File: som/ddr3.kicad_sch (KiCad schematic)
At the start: 10 parts, among them U2 AS4C256M16D3, U3 AS4C256M16D3

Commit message: Le DDR3 control traces
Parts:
- C1, C2: footprint Capacitor_SMD:C_0402_1005Metric_Pad0.74x0.62mm_HandSolder -> Capacitor_SMD:C_0402_1005Metric
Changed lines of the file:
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@@
 			)
 		)
-		(property "Footprint" "Capacitor_SMD:C_0402_1005Metric_Pad0.74x0.62mm_HandSolder"
+		(property "Footprint" "Capacitor_SMD:C_0402_1005Metric"
 			(at 147.32 49.53 0)
 			(effects
@@
 			)
 		)
-		(property "Footprint" "Capacitor_SMD:C_0402_1005Metric_Pad0.74x0.62mm_HandSolder"
+		(property "Footprint" "Capacitor_SMD:C_0402_1005Metric"
 			(at 81.28 49.53 0)
 			(effects

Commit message: DDR3 (again)
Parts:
- removed R6, R7, R8, R9: 10k, Resistor_SMD:R_0402_1005Metric_Pad0.72x0.64mm_HandSolder, symbol Device:R_Small
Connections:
- net DDR_VREF: now reaches C2.1, U2.H1 (VREFDQ), U2.M8 (VREFCA)
- net DDR_VREF: now also C1.1, U3.H1 (VREFDQ), U3.M8 (VREFCA)
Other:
- moved on the sheet: C1, C2

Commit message: I really should commit when I make it and not a month later
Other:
- note added: "DDR3L Configuration: 256K*32 Speed: 800 MT/s Impedance: 40 ohm"
- moved on the sheet: C1, C2, R1, R2, U2, U3

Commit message: ok
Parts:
- added C100: 4.7uF, Capacitor_SMD:C_0402_1005Metric, symbol Device:C_Small
- added C97, C99: 100nF, Capacitor_SMD:C_0402_1005Metric, symbol Device:C_Small
- added C98: 1nF, Capacitor_SMD:C_0402_1005Metric, symbol Device:C_Small
- added R17, R18: 10K, Resistor_SMD:R_0402_1005Metric_Pad0.72x0.64mm_HandSolder, symbol Device:R_Small
- added RN1, RN2, RN3, RN4, RN5, RN6, RN7: R_Pack04, Resistor_SMD:R_Array_Concave_4x0402, symbol Device:R_Pack04
- added U9: TPS51200DRC, Package_SON:VSON-10-1EP_3x3mm_P0.5mm_EP1.65x2.4mm, symbol Regulator_Linear:TPS51200DRC
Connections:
- net +1V35: now also R17.2, U9.2 (VLDOIN)
- net DDR_A0: now also RN5.7 (R2.2)
- net DDR_A1: now also RN1.8 (R1.2)
- net DDR_A10: now also RN3.5 (R4.2)
- net DDR_A11: now also RN1.6 (R3.2)
- net DDR_A12: now also RN2.8 (R1.2)
- net DDR_A13: now also RN4.8 (R1.2)
- net DDR_A14: now also RN1.5 (R4.2)
- net DDR_A2: now also RN4.5 (R4.2)
- net DDR_A3: now also RN5.6 (R3.2)
- net DDR_A4: now also RN2.6 (R3.2)
- net DDR_A5: now also RN5.8 (R1.2)
- net DDR_A6: now also RN2.5 (R4.2)
- net DDR_A7: now also RN4.6 (R3.2)
- net DDR_A8: now also RN1.7 (R2.2)
- net DDR_A9: now also RN4.7 (R2.2)
- net DDR_BA0: now also RN5.5 (R4.2)
- net DDR_BA1: now also RN2.7 (R2.2)
- net DDR_BA2: now also RN6.8 (R1.2)
- net DDR_CLK+: now also RN3.8 (R1.2)
- net DDR_CLK-: now also RN3.7 (R2.2)
- net DDR_CLK_E: now also RN3.6 (R3.2)
- net DDR_ODT: now also RN6.6 (R3.2)
- net DDR_VREF: now also C99.2, U9.6 (REFOUT)
- net GND: now also C100.1, C98.2, C99.1, R18.2, U9.11 (GND), U9.4 (GND), U9.8 (GND)
- net ~{DDR_CAS}: now also RN7.7 (R2.2)
- net ~{DDR_CS}: now also RN6.7 (R2.2)
- net ~{DDR_RAS}: now also RN7.8 (R1.2)
- net ~{DDR_WE}: now also RN7.6 (R3.2)
- new net: C98.1, R17.1, R18.1, U9.1 (REFIN)
- new net: C97.1, RN3.1 (R1.1), RN3.2 (R2.1)
- new net +3V3: C100.2, U9.10 (VIN), U9.7 (EN)
- new net V_{TT}: C97.2, RN1.1 (R1.1), RN1.2 (R2.1), RN1.3 (R3.1), RN1.4 (R4.1), RN2.1 (R1.1), RN2.2 (R2.1), RN2.3 (R3.1), RN2.4 (R4.1), RN3.3 (R3.1), RN3.4 (R4.1), RN4.1 (R1.1), RN4.2 (R2.1), RN4.3 (R3.1), RN4.4 (R4.1), RN5.1 (R1.1), RN5.2 (R2.1), RN5.3 (R3.1), RN5.4 (R4.1), RN6.1 (R1.1), RN6.2 (R2.1), RN6.3 (R3.1), RN7.1 (R1.1), RN7.2 (R2.1), RN7.3 (R3.1), U9.3 (VO), U9.5 (VOSNS)
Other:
- note added: "DDR3L Configuration: 256K*32 Speed: 800 MT/s Impedance: 40 ohm Termination: 40 ohm AC termination: 40 ohm, 100nF"
- note removed: "DDR3L Configuration: 256K*32 Speed: 800 MT/s Impedance: 40 ohm"
- moved on the sheet: C1, C2, R1, R2, U2, U3

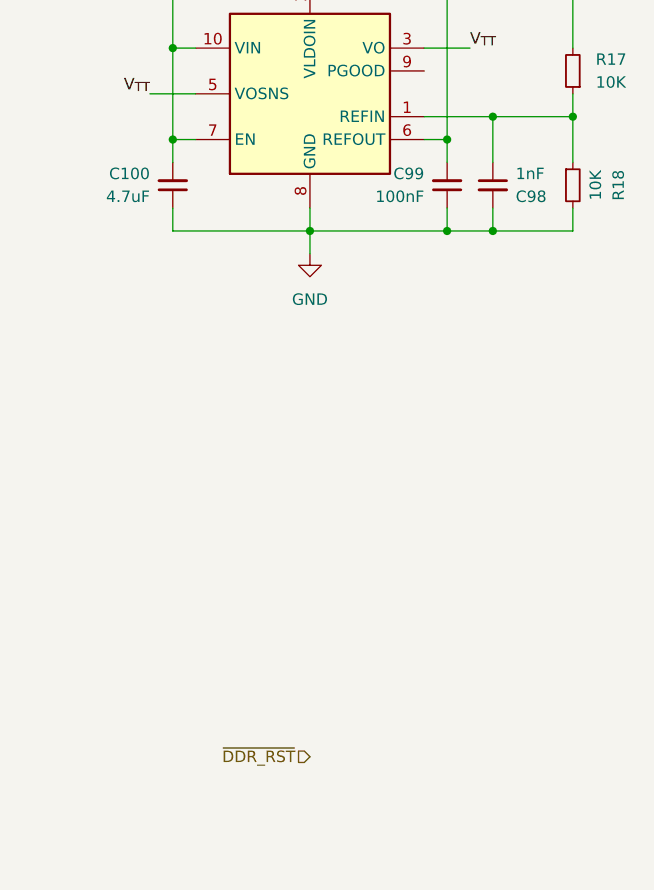
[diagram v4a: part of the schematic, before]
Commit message: Work on GTP and power supplies for it
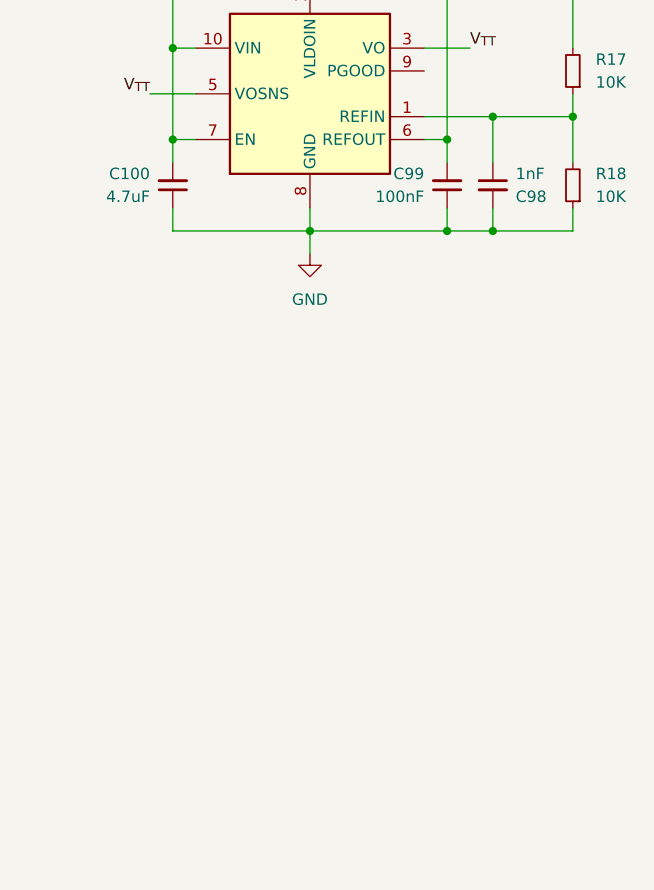
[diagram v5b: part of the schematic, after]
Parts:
- R17, R18: footprint Resistor_SMD:R_0402_1005Metric_Pad0.72x0.64mm_HandSolder -> Resistor_SMD:R_0402_1005Metric
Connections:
- net GND: now also R18.1; no longer R18.2
- net at C98.1, R17.1, U9.1 (REFIN): now also R18.2; no longer R18.1
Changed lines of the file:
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@@
-		)
-	)
-	(hierarchical_label "~{DDR_RST}"
-		(shape input)
-		(at 240.03 138.43 180)
-		(fields_autoplaced yes)
-		(effects
-			(font
-				(size 1.27 1.27)
-			)
-			(justify right)
 		)
 	)
@@
 	)
 	(symbol
+		(lib_id "Device:R_Small")
+		(at 269.24 74.93 180)
+		(unit 1)
+		(exclude_from_sim no)
+		(in_bom yes)
+		(on_board yes)
+		(dnp no)
+		(property "Reference" "R18"
+			(at 271.78 73.6599 0)
+			(effects
+				(font
+					(size 1.27 1.27)
+				)
+				(justify right)
+			)
+		)
+		(property "Value" "10K"
+			(at 271.78 76.1999 0)
+			(effects
+				(font
+					(size 1.27 1.27)
+				)
+				(justify right)
+			)
+		)
+		(property "Footprint" "Resistor_SMD:R_0402_1005Metric"
+			(at 269.24 74.93 0)
+			(effects
+				(font
+					(size 1.27 1.27)
+				)
+				(hide yes)
+			)
+		)
+		(property "Datasheet" "~"
+			(at 269.24 74.93 0)
+			(effects
+				(font
+					(size 1.27 1.27)
+				)
+				(hide yes)
+			)
+		)
+		(property "Description" "Resistor, small symbol"
+			(at 269.24 74.93 0)
+			(effects
+				(font
+					(size 1.27 1.27)
+				)
+				(hide yes)
+			)
+		)
+		(pin "2"
+		)
+		(pin "1"
+		)
+		(instances
+			(project "pixieboard"
+				(path "/e7142f2b-5d92-4ad9-8024-bfc94c5783c1/57afc700-82e6-45de-a8f3-81fb003e9961"
+					(reference "R18")
+					(unit 1)
+				)
+			)
+		)
+	)
+	(symbol
 		(lib_id "Device:R_Pack04")
 		(at 181.61 63.5 90)
@@
 			)
 		)
-		(property "Footprint" "Resistor_SMD:R_0402_1005Metric_Pad0.72x0.64mm_HandSolder"
+		(property "Footprint" "Resistor_SMD:R_0402_1005Metric"
 			(at 269.24 62.23 0)
 			(effects
@@
 					(unit 1)
 				)
-			)
-		)
-	)
-	(symbol
-		(lib_id "Device:R_Small")
-		(at 269.24 74.93 0)
-		(unit 1)
-		(exclude_from_sim no)
-		(in_bom yes)
-		(on_board yes)
-		(dnp no)
-		(property "Reference" "R18"
-			(at 274.32 74.93 90)
-			(effects
-				(font
-					(size 1.27 1.27)
-				)
-			)
-		)
-		(property "Value" "10K"
-			(at 271.78 74.93 90)
-			(effects
-				(font
-					(size 1.27 1.27)
-				)
-			)
-		)
-		(property "Footprint" "Resistor_SMD:R_0402_1005Metric_Pad0.72x0.64mm_HandSolder"
-			(at 269.24 74.93 0)
-			(effects
-				(font
-					(size 1.27 1.27)
-				)
-				(hide yes)
-			)
-		)
-		(property "Datasheet" "~"
-			(at 269.24 74.93 0)
-			(effects
-				(font
-					(size 1.27 1.27)
-				)
-				(hide yes)
-			)
-		)
-		(property "Description" "Resistor, small symbol"
-			(at 269.24 74.93 0)
-			(effects
-				(font
-					(size 1.27 1.27)
-				)
-				(hide yes)
-			)
-		)
-		(pin "2"
-		)
-		(pin "1"
-		)
-		(instances
-			(project "pixieboard"
-				(path "/e7142f2b-5d92-4ad9-8024-bfc94c5783c1/57afc700-82e6-45de-a8f3-81fb003e9961"
-					(reference "R18")
-					(unit 1)
-				)

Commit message: idk
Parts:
- RN1, RN2, RN3, RN4, RN5, RN6, RN7: LCSC part number (none) -> C136844
- U2, U3: LCSC part number (none) -> C2982171
- U9: LCSC part number (none) -> C34771
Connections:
- net V_{TT}: now also RN7.4 (R4.1)
- net ~{DDR_RST}: now also RN7.5 (R4.2)
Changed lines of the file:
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@@
 	)
 	(junction
+		(at 196.85 137.16)
+		(diameter 0)
+		(color 0 0 0 0)
+	)
+	(junction
 		(at 196.85 63.5)
 		(diameter 0)
@@
 	(wire
 		(pts
+			(xy 196.85 137.16) (xy 196.85 139.7)
+		)
+		(stroke
+			(width 0)
+			(type default)
+		)
+	)
+	(wire
+		(pts
 			(xy 196.85 101.6) (xy 196.85 104.14)
 		)
@@
 	(wire
 		(pts
-			(xy 196.85 132.08) (xy 196.85 139.7)
+			(xy 196.85 132.08) (xy 196.85 137.16)
 		)
 		(stroke
@@
 	(wire
 		(pts
+			(xy 186.69 137.16) (xy 196.85 137.16)
+		)
+		(stroke
+			(width 0)
+			(type default)
+		)
+	)
+	(wire
+		(pts
 			(xy 54.61 53.34) (xy 54.61 55.88)
 		)
@@
 		)
 	)
+	(hierarchical_label "~{DDR_RST}"
+		(shape input)
+		(at 176.53 137.16 180)
+		(fields_autoplaced yes)
+		(effects
+			(font
+				(size 1.27 1.27)
+			)
+			(justify right)
+		)
+	)
 	(hierarchical_label "DDR_A11"
 		(shape input)
@@
 			)
 		)
+		(property "LCSC part number" "C2982171"
+			(at 49.53 99.06 0)
+			(effects
+				(font
+					(size 1.27 1.27)
+				)
+				(hide yes)
+			)
+		)
 		(pin "C2"
 		)
@@
 			)
 		)
+		(property "LCSC part number" "C34771"
+			(at 240.03 64.77 0)
+			(effects
+				(font
+					(size 1.27 1.27)
+				)
+				(hide yes)
+			)
+		)
 		(pin "7"
 		)
@@
 			)
 		)
+		(property "LCSC part number" "C136844"
+			(at 181.61 63.5 90)
+			(effects
+				(font
+					(size 1.27 1.27)
+				)
+				(hide yes)
+			)
+		)
 		(pin "6"
 		)
@@
 			)
 		)
+		(property "LCSC part number" "C136844"
+			(at 181.61 114.3 90)
+			(effects
+				(font
+					(size 1.27 1.27)
+				)
+				(hide yes)
+			)
+		)
 		(pin "6"
 		)
@@
 			)
 		)
+		(property "LCSC part number" "C136844"
+			(at 181.61 76.2 90)
+			(effects
+				(font
+					(size 1.27 1.27)
+				)
+				(hide yes)
+			)
+		)
 		(pin "6"
 		)
@@
 			)
 		)
+		(property "LCSC part number" "C136844"
+			(at 181.61 127 90)
+			(effects
+				(font
+					(size 1.27 1.27)
+				)
+				(hide yes)
+			)
+		)
 		(pin "6"
 		)
@@
 			)
 		)
+		(property "LCSC part number" "C136844"
+			(at 181.61 88.9 90)
+			(effects
+				(font
+					(size 1.27 1.27)
+				)
+				(hide yes)
+			)
+		)
 		(pin "6"
 		)
@@
 			)
 		)
+		(property "LCSC part number" "C136844"
+			(at 181.61 101.6 90)
+			(effects
+				(font
+					(size 1.27 1.27)
+				)
+				(hide yes)
+			)
+		)
 		(pin "6"
 		)
@@
 			)
 		)
+		(property "LCSC part number" "C2982171"
+			(at 115.57 99.06 0)
+			(effects
+				(font
+					(size 1.27 1.27)
+				)
+				(hide yes)
+			)
+		)
 		(pin "C2"
 		)
@@
 			(effects
 				(font
+					(size 1.27 1.27)
+				)
+				(hide yes)
+			)
+		)
+		(property "LCSC part number" "C136844"
+			(at 181.61 139.7 90)
+			(effects
+				(font
